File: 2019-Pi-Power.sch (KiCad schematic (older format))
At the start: 25 parts, among them J1 Barrel_Jack_Switch, J2 USB_A, J3 USB_A, J4 Conn_02x04_Odd_Even, J5 Conn_01x04, J6 Conn_01x04, J7 Conn_01x04, J8 Conn_02x02_Odd_Even, P1 Conn_02x20_Odd_Even, U1 MP1584

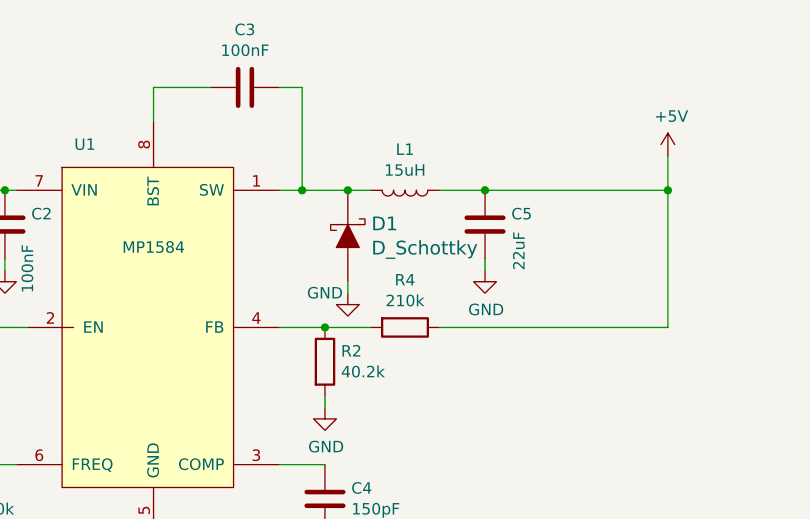
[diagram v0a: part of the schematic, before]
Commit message: Update component Values
Add BOM
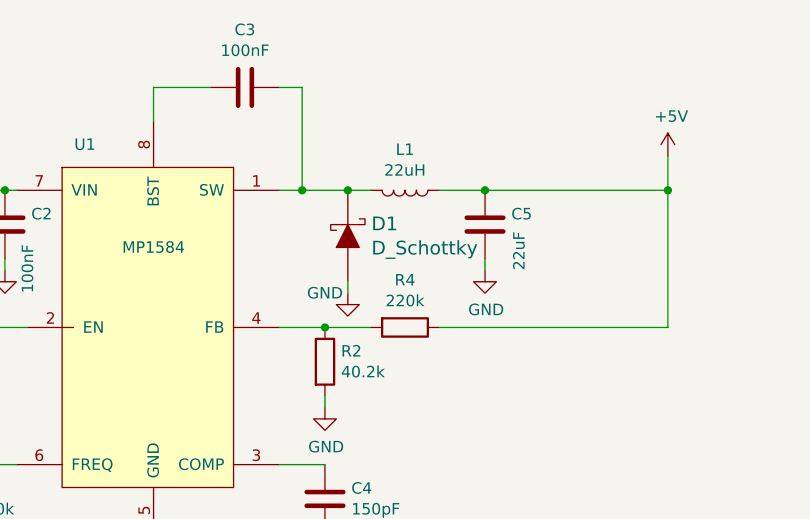
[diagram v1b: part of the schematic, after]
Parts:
- L1: value 15uH -> 22uH
- R4: value 210k -> 220k
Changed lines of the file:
@@
 P 4100 1300
 F 0 "L1" V 3922 1300 50  0000 C CNN
-F 1 "15uH" V 4013 1300 50  0000 C CNN
+F 1 "22uH" V 4013 1300 50  0000 C CNN
 F 2 "Inductors_SMD:L_10.4x10.4_H4.8" H 4100 1300 50  0001 C CNN
 F 3 "~" H 4100 1300 50  0001 C CNN
@@
 P 4100 1900
 F 0 "R4" V 3893 1900 50  0000 C CNN
-F 1 "210k" V 3984 1900 50  0000 C CNN
+F 1 "220k" V 3984 1900 50  0000 C CNN
 F 2 "Resistors_SMD:R_0603" V 4030 1900 50  0001 C CNN
 F 3 "~" H 4100 1900 50  0001 C CNN
